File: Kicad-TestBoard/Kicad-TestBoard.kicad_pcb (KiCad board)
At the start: 2 copper layers, 50 x 100 mm, 40 parts, among them CON1 Power 6V-12V, J1 DB9 RS-232 Female, P1 Power 6V-12V, P2 Debug, P4 Arduino, P5 AVR Programmer, P6 RS-232, Q1 Association, Q2 On_Sleep, Q3 Commissioning, SW1 Reset, SW2 Commissioning, U1 78L05, U2 MAX232

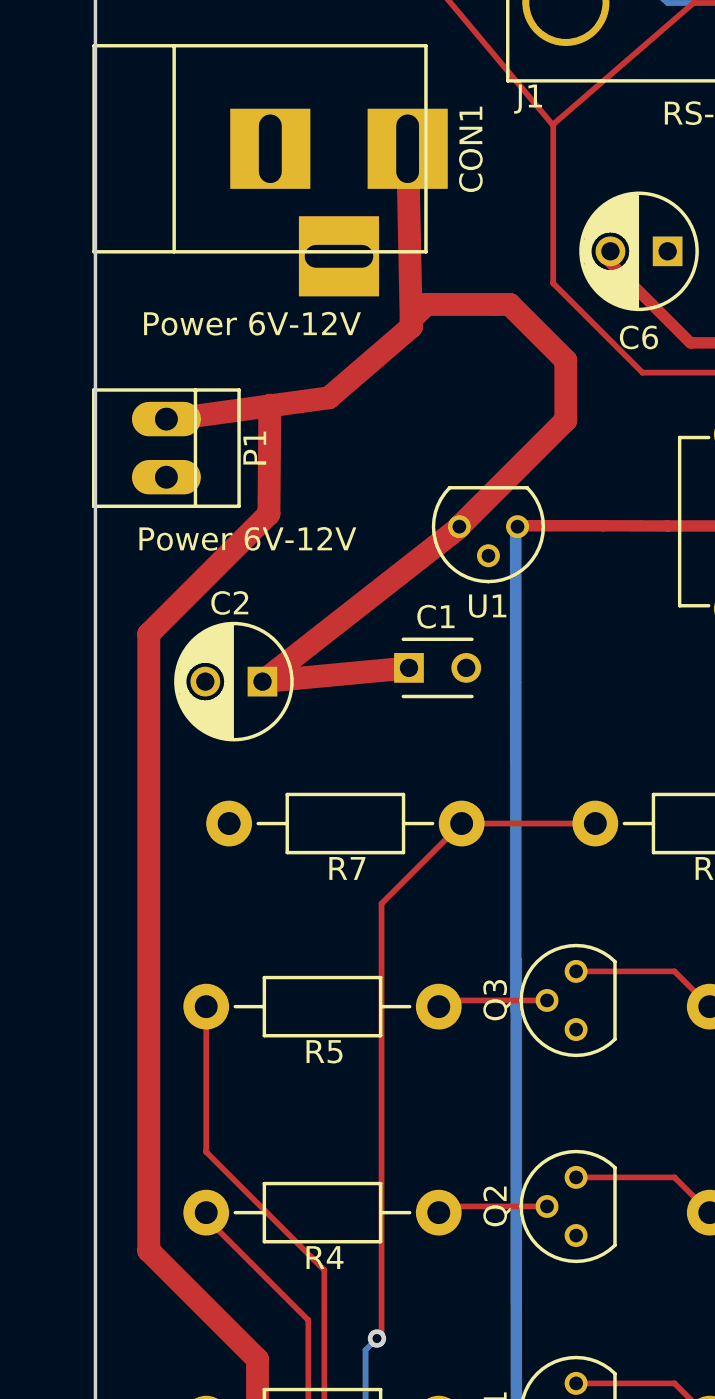
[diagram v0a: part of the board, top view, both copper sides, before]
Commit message: Minor reroute of power on testboard
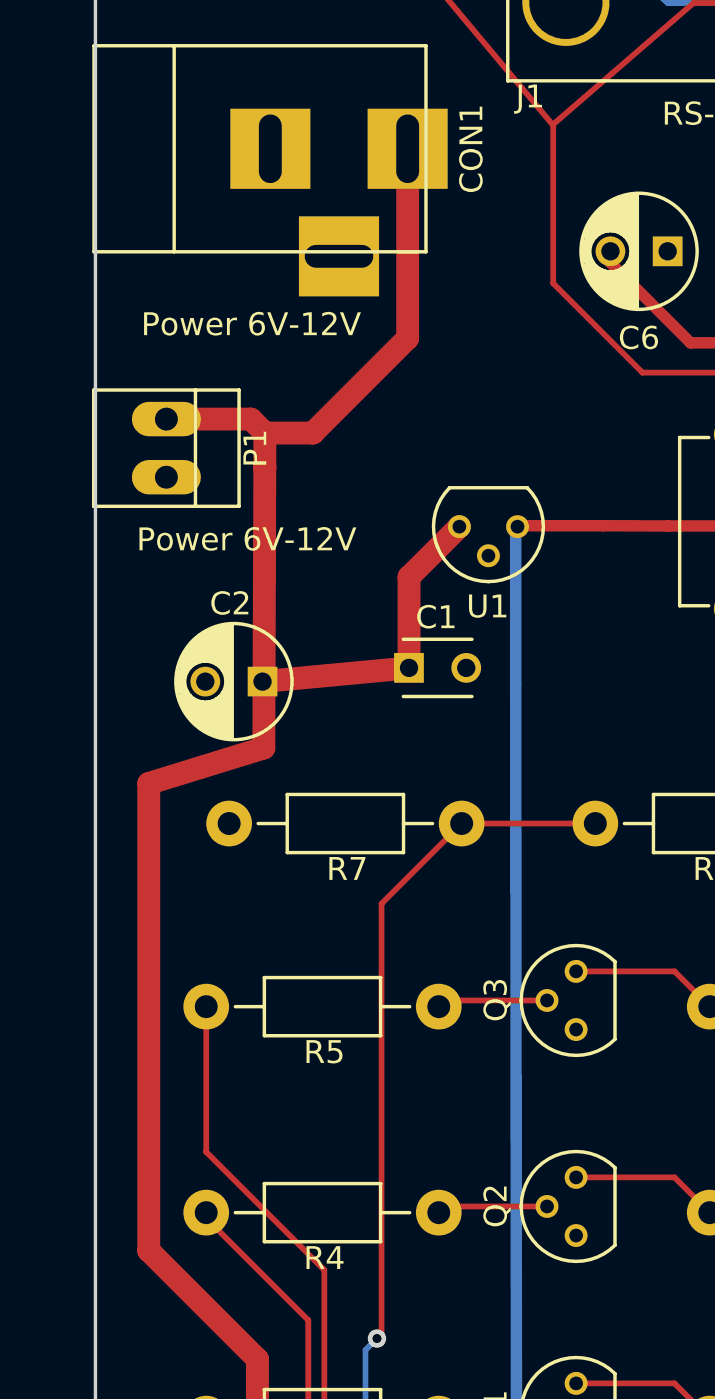
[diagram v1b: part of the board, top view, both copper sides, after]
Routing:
- net Net-(C1-Pad1): track 131.5 -> 111.4 mm
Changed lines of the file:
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@@
     (thickness 1.6)
     (drawings 18)
-    (tracks 192)
+    (tracks 190)
     (zones 0)
     (modules 40)
@@
   (page A4)
   (layers
-    (0 F.Cu signal hide)
-    (31 B.Cu signal hide)
+    (0 F.Cu signal)
+    (31 B.Cu signal)
     (32 B.Adhes user hide)
     (33 F.Adhes user hide)
@@
   )
   (setup
-    (last_trace_width 0.25)
+    (last_trace_width 1)
     (user_trace_width 0.5)
     (user_trace_width 1)
@@
   (segment (start 158.8 146.3) (end 180.3 146.3) (width 0.25) (layer F.Cu) (net 39))
   (segment (start 154.84 122.64) (end 155.6 123.4) (width 0.25) (layer F.Cu) (net 39))
+  (segment (start 157.399753 77.939753) (end 159.500247 77.939753) (width 1) (layer F.Cu) (net 42))
+  (segment (start 163.64014 73.79986) (end 163.64014 65.52) (width 1) (layer F.Cu) (net 42) (status 800000))
+  (segment (start 159.500247 77.939753) (end 163.64014 73.79986) (width 1) (layer F.Cu) (net 42))
+  (segment (start 157.399753 79.459651) (end 157.399753 77.939753) (width 1) (layer F.Cu) (net 42))
+  (segment (start 156.79 77.33) (end 153.1 77.33) (width 1) (layer F.Cu) (net 42) (status 800000))
+  (segment (start 157.399753 77.939753) (end 156.79 77.33) (width 1) (layer F.Cu) (net 42))
+  (segment (start 163.7 88.2) (end 163.7 84.23) (width 1) (layer F.Cu) (net 42) (status 400000))
+  (segment (start 163.7 84.23) (end 165.9 82.03) (width 1) (layer F.Cu) (net 42) (status 800000))
   (segment (start 163.22 144.46) (end 159.7 144.5) (width 1) (layer F.Cu) (net 42))
-  (segment (start 157.58 81.47) (end 157.62 76.72) (width 1) (layer F.Cu) (net 42))
-  (segment (start 152.33 86.72) (end 157.58 81.47) (width 1) (layer F.Cu) (net 42))
-  (segment (start 152.33 113.66) (end 152.33 86.72) (width 1) (layer F.Cu) (net 42))
+  (segment (start 157.356349 91.699012) (end 157.399753 79.459651) (width 1) (layer F.Cu) (net 42))
+  (segment (start 157.399753 79.459651) (end 157.4 79.39) (width 1) (layer F.Cu) (net 42))
+  (segment (start 152.33 93.25) (end 157.356349 91.699012) (width 1) (layer F.Cu) (net 42))
+  (segment (start 152.33 113.66) (end 152.33 93.25) (width 1) (layer F.Cu) (net 42))
   (segment (start 157.08 118.41) (end 152.33 113.66) (width 1) (layer F.Cu) (net 42))
   (segment (start 157.08 141.88) (end 157.08 118.41) (width 1) (layer F.Cu) (net 42))
   (segment (start 159.7 144.5) (end 157.08 141.88) (width 1) (layer F.Cu) (net 42))
-  (segment (start 167.47 72.32) (end 168.1 72.32) (width 1) (layer F.Cu) (net 42))
-  (segment (start 168.1 72.32) (end 170.55 74.77) (width 1) (layer F.Cu) (net 42))
-  (segment (start 170.55 77.38) (end 165.9 82.03) (width 1) (layer F.Cu) (net 42))
-  (segment (start 170.55 74.77) (end 170.55 77.38) (width 1) (layer F.Cu) (net 42))
-  (segment (start 163.8 72.97) (end 163.8 73.3) (width 1) (layer F.Cu) (net 42))
-  (segment (start 164.45 72.32) (end 163.8 72.97) (width 1) (layer F.Cu) (net 42))
-  (segment (start 167.47 72.32) (end 164.45 72.32) (width 1) (layer F.Cu) (net 42))
-  (segment (start 163.8 73.3) (end 160.2 76.4) (width 1) (layer F.Cu) (net 42))
   (segment (start 163.7 88.2) (end 157.3 88.8) (width 1) (layer F.Cu) (net 42))
   (segment (start 157.3 88.8) (end 157.4 88.9) (width 1) (layer F.Cu) (net 42) (status 10))
-  (segment (start 163.64014 65.52) (end 163.8 73.3) (width 1) (layer F.Cu) (net 42))
-  (segment (start 160.2 76.4) (end 152.9 77.4) (width 1) (layer F.Cu) (net 42))
-  (segment (start 165.89 82.07) (end 157.3 88.8) (width 1) (layer F.Cu) (net 42) (status 10))
   (segment (start 157.3 88.8) (end 157.3 88.8) (width 1) (layer F.Cu) (net 42) (status 20))
   (zone (net 2) (net_name Earth) (layer B.Cu) (hatch edge 0.508)

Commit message: Minor tweaks on the PCBs ready to manufacture
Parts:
- moved G*** 1.01 mm to (180.9, 52.9)
- moved P6 0.50 mm to (161.4, 53.3)
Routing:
- net Net-(J1-Pad3): track 52.9 -> 53.4 mm
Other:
- board text added: "(Arduino)"
- board text added: "Do NOT link if Battery present"
- board text added: "Ground Count"
- board text removed: "Count (Arduino)"
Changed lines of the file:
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@@
-(kicad_pcb (version 4) (host pcbnew 4.0.5-e0-6337~49~ubuntu14.04.1)
+(kicad_pcb (version 4) (host pcbnew 4.0.5-e0-6337~49~ubuntu16.04.1)
   (general
     (links 73)
-    (no_connects 1)
+    (no_connects 23)
     (area 143.5 46.5 207.200001 156.000001)
     (thickness 1.6)
-    (drawings 18)
+    (drawings 20)
     (tracks 190)
     (zones 0)
@@
   )
   (setup
-    (last_trace_width 1)
+    (last_trace_width 0.25)
     (user_trace_width 0.5)
     (user_trace_width 1)
@@
   )
   (module photodiode:Xerofill-Logo-Small (layer F.Cu)
-    (at 181.9 53.05)
+    (at 180.9 52.9)
     (fp_text reference G*** (at 0 0) (layer F.SilkS) hide
       (effects (font (thickness 0.3)))
@@
   (module Testboard:pin_header_2mm_2x6_shrouded (layer F.Cu)
     (at 178.8 143.5)
-    (fp_text reference P2 (at -6 4) (layer F.SilkS)
+    (fp_text reference P2 (at -5.4 4.2) (layer F.SilkS)
       (effects (font (size 1 1) (thickness 0.15)))
     )
@@
   )
   (module Testboard:PINHEAD1-4 (layer F.Cu)
-    (at 161.9 53.3 180)
+    (at 161.4 53.3 180)
     (attr virtual)
-    (fp_text reference P6 (at -6.4 0.5 180) (layer F.SilkS)
+    (fp_text reference P6 (at 4.5 -4.3 180) (layer F.SilkS)
       (effects (font (size 1 1) (thickness 0.15)))
     )
@@
     (descr "Connecteurs 1 pin")
     (tags "CONN DEV")
-    (fp_text reference W1 (at 0 -1.7) (layer F.SilkS)
+    (fp_text reference W1 (at 0.2 1.88) (layer F.SilkS)
       (effects (font (size 0.8 0.8) (thickness 0.15)))
     )
@@
       (net 42 "Net-(C1-Pad1)"))
   )
+  (gr_text "Ground\n\nCount" (at 152.9 127.4) (layer F.SilkS)
+    (effects (font (size 1 1) (thickness 0.2)))
+  )
+  (gr_text "Do NOT link if\nBattery present" (at 164.9 140.4) (layer F.SilkS)
+    (effects (font (size 1 1) (thickness 0.25)))
+  )
   (gr_text "Version 2\nK. Sarkies\n05/12/2016" (at 192 141.66) (layer F.SilkS)
     (effects (font (size 1 1) (thickness 0.2)))
@@
     (effects (font (size 1 1) (thickness 0.25)))
   )
-  (gr_text "Watermeter Test Board" (at 186.29 138.02) (layer F.SilkS)
-    (effects (font (size 1 1) (thickness 0.25)))
-  )
-  (gr_text RS-232 (at 162.2 57.6) (layer F.SilkS)
+  (gr_text "Watermeter Test Board" (at 185.9 137.6) (layer F.SilkS)
+    (effects (font (size 1.4 1.4) (thickness 0.35)))
+  )
+  (gr_text RS-232 (at 161.6 57.6) (layer F.SilkS)
     (effects (font (size 1 1) (thickness 0.2)))
   )
@@
     (effects (font (size 1 1) (thickness 0.2)))
   )
-  (gr_text "Count (Arduino)" (at 156.7 143) (layer F.SilkS)
+  (gr_text "(Arduino)" (at 153.9 143.5) (layer F.SilkS)
     (effects (font (size 1 1) (thickness 0.2)))
   )
@@
   (segment (start 185.794 57.726) (end 185.624 57.726) (width 0.25) (layer F.Cu) (net 14) (status 30))
   (segment (start 185.624 57.726) (end 184.2 59.15) (width 0.25) (layer F.Cu) (net 14) (status 10))
-  (segment (start 170 64.5) (end 160.63 53.3) (width 0.25) (layer F.Cu) (net 14) (status 20))
+  (segment (start 170 64.5) (end 160.2 53.6) (width 0.25) (layer F.Cu) (net 14) (status 20))
   (segment (start 176.131253 59.15) (end 170.003125 64.45) (width 0.25) (layer F.Cu) (net 14))
   (segment (start 184.2 59.15) (end 176.131253 59.15) (width 0.25) (layer F.Cu) (net 14))
@@
   (segment (start 183 57.726) (end 182.724 57.726) (width 0.25) (layer B.Cu) (net 15) (status 30))
   (segment (start 182.724 57.726) (end 181.3 59.15) (width 0.25) (layer B.Cu) (net 15) (status 10))
-  (segment (start 165.9 56.4) (end 163.17 53.05) (width 0.25) (layer B.Cu) (net 15) (status 20))
-  (segment (start 171.8 56.35) (end 165.9 56.4) (width 0.25) (layer B.Cu) (net 15))
+  (segment (start 164.801846 56.302067) (end 162.3 53.5) (width 0.25) (layer B.Cu) (net 15) (status 20))
+  (segment (start 171.8 56.35) (end 164.801846 56.302067) (width 0.25) (layer B.Cu) (net 15))
   (segment (start 175 59.15) (end 171.8 56.35) (width 0.25) (layer B.Cu) (net 15))
   (segment (start 181.3 59.15) (end 175 59.15) (width 0.25) (layer B.Cu) (net 15))
@@
   (segment (start 154.84 122.64) (end 155.6 123.4) (width 0.25) (layer F.Cu) (net 39))
   (segment (start 157.399753 77.939753) (end 159.500247 77.939753) (width 1) (layer F.Cu) (net 42))
-  (segment (start 163.64014 73.79986) (end 163.64014 65.52) (width 1) (layer F.Cu) (net 42) (status 800000))
+  (segment (start 163.64014 73.79986) (end 163.64014 65.52) (width 1) (layer F.Cu) (net 42))
   (segment (start 159.500247 77.939753) (end 163.64014 73.79986) (width 1) (layer F.Cu) (net 42))
   (segment (start 157.399753 79.459651) (end 157.399753 77.939753) (width 1) (layer F.Cu) (net 42))
-  (segment (start 156.79 77.33) (end 153.1 77.33) (width 1) (layer F.Cu) (net 42) (status 800000))
+  (segment (start 156.79 77.33) (end 153.1 77.33) (width 1) (layer F.Cu) (net 42))
   (segment (start 157.399753 77.939753) (end 156.79 77.33) (width 1) (layer F.Cu) (net 42))
-  (segment (start 163.7 88.2) (end 163.7 84.23) (width 1) (layer F.Cu) (net 42) (status 400000))
-  (segment (start 163.7 84.23) (end 165.9 82.03) (width 1) (layer F.Cu) (net 42) (status 800000))
+  (segment (start 163.7 88.2) (end 163.7 84.23) (width 1) (layer F.Cu) (net 42))
+  (segment (start 163.7 84.23) (end 165.9 82.03) (width 1) (layer F.Cu) (net 42))
   (segment (start 163.22 144.46) (end 159.7 144.5) (width 1) (layer F.Cu) (net 42))
   (segment (start 157.356349 91.699012) (end 157.399753 79.459651) (width 1) (layer F.Cu) (net 42))
@@
     (connect_pads (clearance 0.508))
     (min_thickness 0.254)
-    (fill yes (arc_segments 16) (thermal_gap 0.508) (thermal_bridge_width 0.508))
+    (fill (arc_segments 16) (thermal_gap 0.508) (thermal_bridge_width 0.508))
     (polygon
       (pts
@@
     (connect_pads (clearance 0.508))
     (min_thickness 0.254)
-    (fill yes (arc_segments 16) (thermal_gap 0.508) (thermal_bridge_width 0.508))
+    (fill (arc_segments 16) (thermal_gap 0.508) (thermal_bridge_width 0.508))
     (polygon
       (pts
